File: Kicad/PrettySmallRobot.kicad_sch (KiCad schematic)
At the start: 52 parts, among them J1 TYPE-C-31-M-12, J2 S2B-PH-K-S(LF)(SN), J3 S2B-PH-K-S(LF)(SN), J4 S2B-PH-K-S(LF)(SN), SW1 SW_Push, SW2 SW_Push, U1 DRV8837, U2 DRV8837, U3 MCP73831-2ACI_MC, U4 ESP32-S2

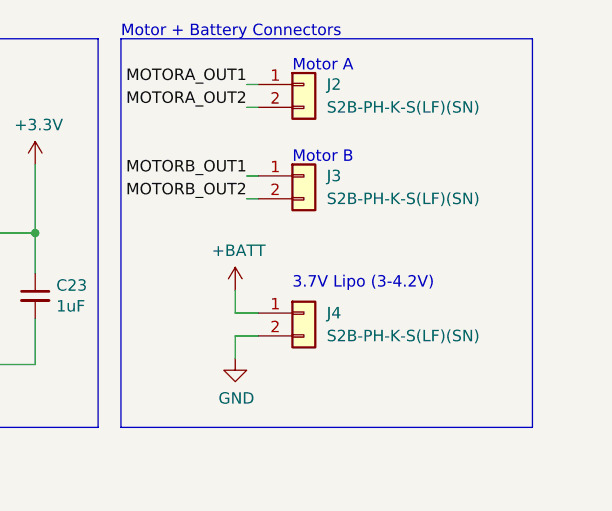
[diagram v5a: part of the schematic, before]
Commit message: replaced jst connectors with smd solder pads
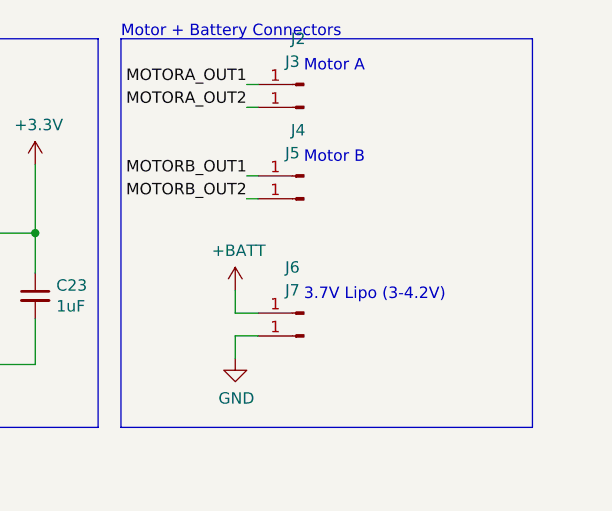
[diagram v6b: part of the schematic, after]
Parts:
- removed J2, J3, J4: S2B-PH-K-S(LF)(SN), Connector_JST:JST_PH_S2B-PH-K_1x02_P2.00mm_Horizontal, symbol Connector_Generic:Conn_01x02
- added J2, J3, J4, J5, J6, J7: (no value), Connector_Wire:SolderWirePad_1x01_SMD_1x2mm, symbol Connector:Conn_01x01_Male
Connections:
- net +BATT: now also J6.1 (Pin_1)
- net GND: now also J7.1 (Pin_1)
- net MOTORA_OUT1: now also J2.1 (Pin_1)
- net MOTORA_OUT2: now also J3.1 (Pin_1)
- net MOTORB_OUT1: now also J4.1 (Pin_1)
- net MOTORB_OUT2: now also J5.1 (Pin_1)
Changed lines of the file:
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@@
     (effects (font (size 1.27 1.27)) (justify left bottom))
   )
-  (text "Motor A" (at 254 20.32 0)
+  (text "Motor A" (at 255.27 20.32 0)
     (effects (font (size 1.27 1.27)) (justify left bottom))
   )
@@
     (effects (font (size 1.27 1.27)) (justify left bottom))
   )
-  (text "Motor B" (at 254 30.48 0)
+  (text "Motor B" (at 255.27 30.48 0)
     (effects (font (size 1.27 1.27)) (justify left bottom))
   )
-  (text "3.7V Lipo (3-4.2V)" (at 254 44.45 0)
+  (text "3.7V Lipo (3-4.2V)" (at 255.27 45.72 0)
     (effects (font (size 1.27 1.27)) (justify left bottom))
   )
@@
   (label "VDD3P3" (at 44.45 179.07 270)
     (effects (font (size 1.27 1.27)) (justify right bottom))
+  )
+  (symbol (lib_id "Connector:Conn_01x01_Male") (at 255.27 49.53 180) (unit 1)
+    (in_bom yes) (on_board yes)
+    (property "Reference" "J7" (id 0) (at 254 44.45 0))
+    (property "Value" "" (id 1) (at 257.81 49.53 0))
+    (property "Footprint" "Connector_Wire:SolderWirePad_1x01_SMD_1x2mm" (id 2) (at 255.27 49.53 0)
+      (effects (font (size 1.27 1.27)) hide)
+    )
+    (property "Datasheet" "~" (id 3) (at 255.27 49.53 0)
+      (effects (font (size 1.27 1.27)) hide)
+    )
+    (pin "1")
   )
   (symbol (lib_id "power:GND") (at 207.01 52.705 0) (unit 1)
@@
     (pin "1")
     (pin "2")
+  )
+  (symbol (lib_id "Connector:Conn_01x01_Male") (at 255.27 46.99 180) (unit 1)
+    (in_bom yes) (on_board yes)
+    (property "Reference" "J6" (id 0) (at 254 41.91 0))
+    (property "Value" "" (id 1) (at 259.08 46.99 0))
+    (property "Footprint" "Connector_Wire:SolderWirePad_1x01_SMD_1x2mm" (id 2) (at 255.27 46.99 0)
+      (effects (font (size 1.27 1.27)) hide)
+    )
+    (property "Datasheet" "~" (id 3) (at 255.27 46.99 0)
+      (effects (font (size 1.27 1.27)) hide)
+    )
+    (pin "1")
   )
   (symbol (lib_id "power:GND") (at 119.38 127 90) (unit 1)
@@
     (pin "2")
   )
-  (symbol (lib_id "Connector_Generic:Conn_01x02") (at 255.27 21.59 0) (unit 1)
-    (in_bom yes) (on_board yes) (fields_autoplaced)
-    (property "Reference" "J2" (id 0) (at 257.81 21.5899 0)
-      (effects (font (size 1.27 1.27)) (justify left))
-    )
-    (property "Value" "S2B-PH-K-S(LF)(SN)" (id 1) (at 257.81 24.1299 0)
-      (effects (font (size 1.27 1.27)) (justify left))
-    )
-    (property "Footprint" "Connector_JST:JST_PH_S2B-PH-K_1x02_P2.00mm_Horizontal" (id 2) (at 255.27 21.59 0)
-      (effects (font (size 1.27 1.27)) hide)
-    )
-    (property "Datasheet" "~" (id 3) (at 255.27 21.59 0)
-      (effects (font (size 1.27 1.27)) hide)
-    )
-    (property "LCSC" "C173752" (id 4) (at 255.27 21.59 0)
-      (effects (font (size 1.27 1.27)) hide)
-    )
-    (pin "1")
-    (pin "2")
-  )
   (symbol (lib_id "power:+3.3V") (at 54.61 176.53 0) (unit 1)
     (in_bom yes) (on_board yes)
@@
     (pin "2")
   )
-  (symbol (lib_id "Connector_Generic:Conn_01x02") (at 255.27 46.99 0) (unit 1)
-    (in_bom yes) (on_board yes) (fields_autoplaced)
-    (property "Reference" "J4" (id 0) (at 257.81 46.9899 0)
-      (effects (font (size 1.27 1.27)) (justify left))
-    )
-    (property "Value" "S2B-PH-K-S(LF)(SN)" (id 1) (at 257.81 49.5299 0)
-      (effects (font (size 1.27 1.27)) (justify left))
-    )
-    (property "Footprint" "Connector_JST:JST_PH_S2B-PH-K_1x02_P2.00mm_Horizontal" (id 2) (at 255.27 46.99 0)
-      (effects (font (size 1.27 1.27)) hide)
-    )
-    (property "Datasheet" "~" (id 3) (at 255.27 46.99 0)
-      (effects (font (size 1.27 1.27)) hide)
-    )
-    (property "LCSC" "C173752" (id 4) (at 255.27 46.99 0)
-      (effects (font (size 1.27 1.27)) hide)
-    )
-    (pin "1")
-    (pin "2")
+  (symbol (lib_id "Connector:Conn_01x01_Male") (at 255.27 24.13 180) (unit 1)
+    (in_bom yes) (on_board yes)
+    (property "Reference" "J3" (id 0) (at 254 19.05 0))
+    (property "Value" "" (id 1) (at 260.35 24.13 0))
+    (property "Footprint" "Connector_Wire:SolderWirePad_1x01_SMD_1x2mm" (id 2) (at 255.27 24.13 0)
+      (effects (font (size 1.27 1.27)) hide)
+    )
+    (property "Datasheet" "~" (id 3) (at 255.27 24.13 0)
+      (effects (font (size 1.27 1.27)) hide)
+    )
+    (pin "1")
   )
   (symbol (lib_id "power:+3.3V") (at 67.31 176.53 0) (unit 1)
@@
     )
     (property "Datasheet" "" (id 3) (at 86.36 46.99 0)
+      (effects (font (size 1.27 1.27)) hide)
+    )
+    (pin "1")
+  )
+  (symbol (lib_id "Connector:Conn_01x01_Male") (at 255.27 21.59 180) (unit 1)
+    (in_bom yes) (on_board yes)
+    (property "Reference" "J2" (id 0) (at 254.635 16.51 0))
+    (property "Value" "" (id 1) (at 260.35 21.59 0))
+    (property "Footprint" "Connector_Wire:SolderWirePad_1x01_SMD_1x2mm" (id 2) (at 255.27 21.59 0)
+      (effects (font (size 1.27 1.27)) hide)
+    )
+    (property "Datasheet" "~" (id 3) (at 255.27 21.59 0)
       (effects (font (size 1.27 1.27)) hide)
     )
@@
     (pin "9")
   )
-  (symbol (lib_id "Connector_Generic:Conn_01x02") (at 255.27 31.75 0) (unit 1)
-    (in_bom yes) (on_board yes) (fields_autoplaced)
-    (property "Reference" "J3" (id 0) (at 257.81 31.7499 0)
-      (effects (font (size 1.27 1.27)) (justify left))
-    )
-    (property "Value" "S2B-PH-K-S(LF)(SN)" (id 1) (at 257.81 34.2899 0)
-      (effects (font (size 1.27 1.27)) (justify left))
-    )
-    (property "Footprint" "Connector_JST:JST_PH_S2B-PH-K_1x02_P2.00mm_Horizontal" (id 2) (at 255.27 31.75 0)
-      (effects (font (size 1.27 1.27)) hide)
-    )
-    (property "Datasheet" "~" (id 3) (at 255.27 31.75 0)
-      (effects (font (size 1.27 1.27)) hide)
-    )
-    (property "LCSC" "C173752" (id 4) (at 255.27 31.75 0)
-      (effects (font (size 1.27 1.27)) hide)
-    )
-    (pin "1")
-    (pin "2")
-  )
   (symbol (lib_id "power:+3.3V") (at 208.28 148.59 0) (unit 1)
     (in_bom yes) (on_board yes)
@@
     (pin "2")
   )
+  (symbol (lib_id "Connector:Conn_01x01_Male") (at 255.27 34.29 180) (unit 1)
+    (in_bom yes) (on_board yes)
+    (property "Reference" "J5" (id 0) (at 254 29.21 0))
+    (property "Value" "" (id 1) (at 260.35 34.29 0))
+    (property "Footprint" "Connector_Wire:SolderWirePad_1x01_SMD_1x2mm" (id 2) (at 255.27 34.29 0)
+      (effects (font (size 1.27 1.27)) hide)
+    )
+    (property "Datasheet" "~" (id 3) (at 255.27 34.29 0)
+      (effects (font (size 1.27 1.27)) hide)
+    )
+    (pin "1")
+  )
   (symbol (lib_id "Device:C_Small") (at 78.74 180.34 0) (unit 1)
     (in_bom yes) (on_board yes)
@@
     (pin "1")
     (pin "2")
+  )
+  (symbol (lib_id "Connector:Conn_01x01_Male") (at 255.27 31.75 180) (unit 1)
+    (in_bom yes) (on_board yes)
+    (property "Reference" "J4" (id 0) (at 254.635 26.67 0))
+    (property "Value" "" (id 1) (at 260.35 31.75 0))
+    (property "Footprint" "Connector_Wire:SolderWirePad_1x01_SMD_1x2mm" (id 2) (at 255.27 31.75 0)
+      (effects (font (size 1.27 1.27)) hide)
+    )
+    (property "Datasheet" "~" (id 3) (at 255.27 31.75 0)
+      (effects (font (size 1.27 1.27)) hide)
+    )
+    (pin "1")
   )
   (symbol (lib_id "Connector:TestPoint") (at 219.71 38.1 0) (unit 1)
@@
       (reference "J1") (unit 1) (value "TYPE-C-31-M-12") (footprint "kicad_footprints:HRO_TYPE-C-31-M-12")
     )
-    (path "/3df40196-e4fa-42be-bb30-c5850f257a4a"
-      (reference "J2") (unit 1) (value "S2B-PH-K-S(LF)(SN)") (footprint "Connector_JST:JST_PH_S2B-PH-K_1x02_P2.00mm_Horizontal")
-    )
-    (path "/8c3a71db-8570-4a26-8abb-7b253c8386f5"
-      (reference "J3") (unit 1) (value "S2B-PH-K-S(LF)(SN)") (footprint "Connector_JST:JST_PH_S2B-PH-K_1x02_P2.00mm_Horizontal")
-    )
-    (path "/6502a99f-049b-4441-92af-fda3c2641b16"
-      (reference "J4") (unit 1) (value "S2B-PH-K-S(LF)(SN)") (footprint "Connector_JST:JST_PH_S2B-PH-K_1x02_P2.00mm_Horizontal")
+    (path "/7a0e3aeb-7d38-4968-abed-3c937ea7d594"
+      (reference "J2") (unit 1) (value "MOTORA_1") (footprint "Connector_Wire:SolderWirePad_1x01_SMD_1x2mm")
+    )
+    (path "/66094016-cb8b-4def-bb4e-08ce9dbd32a0"
+      (reference "J3") (unit 1) (value "MOTORA_2") (footprint "Connector_Wire:SolderWirePad_1x01_SMD_1x2mm")
+    )
+    (path "/c4045a03-fc7b-44a0-8023-e7f7c172c253"
+      (reference "J4") (unit 1) (value "MOTORB_1") (footprint "Connector_Wire:SolderWirePad_1x01_SMD_1x2mm")
+    )
+    (path "/a6744a83-e2fe-461f-99f7-2067ecacb1f9"
+      (reference "J5") (unit 1) (value "MOTORB_2") (footprint "Connector_Wire:SolderWirePad_1x01_SMD_1x2mm")
+    )
+    (path "/25861b43-2ae6-4545-970c-1cadff460964"
+      (reference "J6") (unit 1) (value "BATT+") (footprint "Connector_Wire:SolderWirePad_1x01_SMD_1x2mm")
+    )
+    (path "/029525a0-8a41-486f-a02b-f13993394b49"
+      (reference "J7") (unit 1) (value "GND") (footprint "Connector_Wire:SolderWirePad_1x01_SMD_1x2mm")
     )
     (path "/705dc02d-e1e2-48cd-b58e-8d1e3dfceb42"

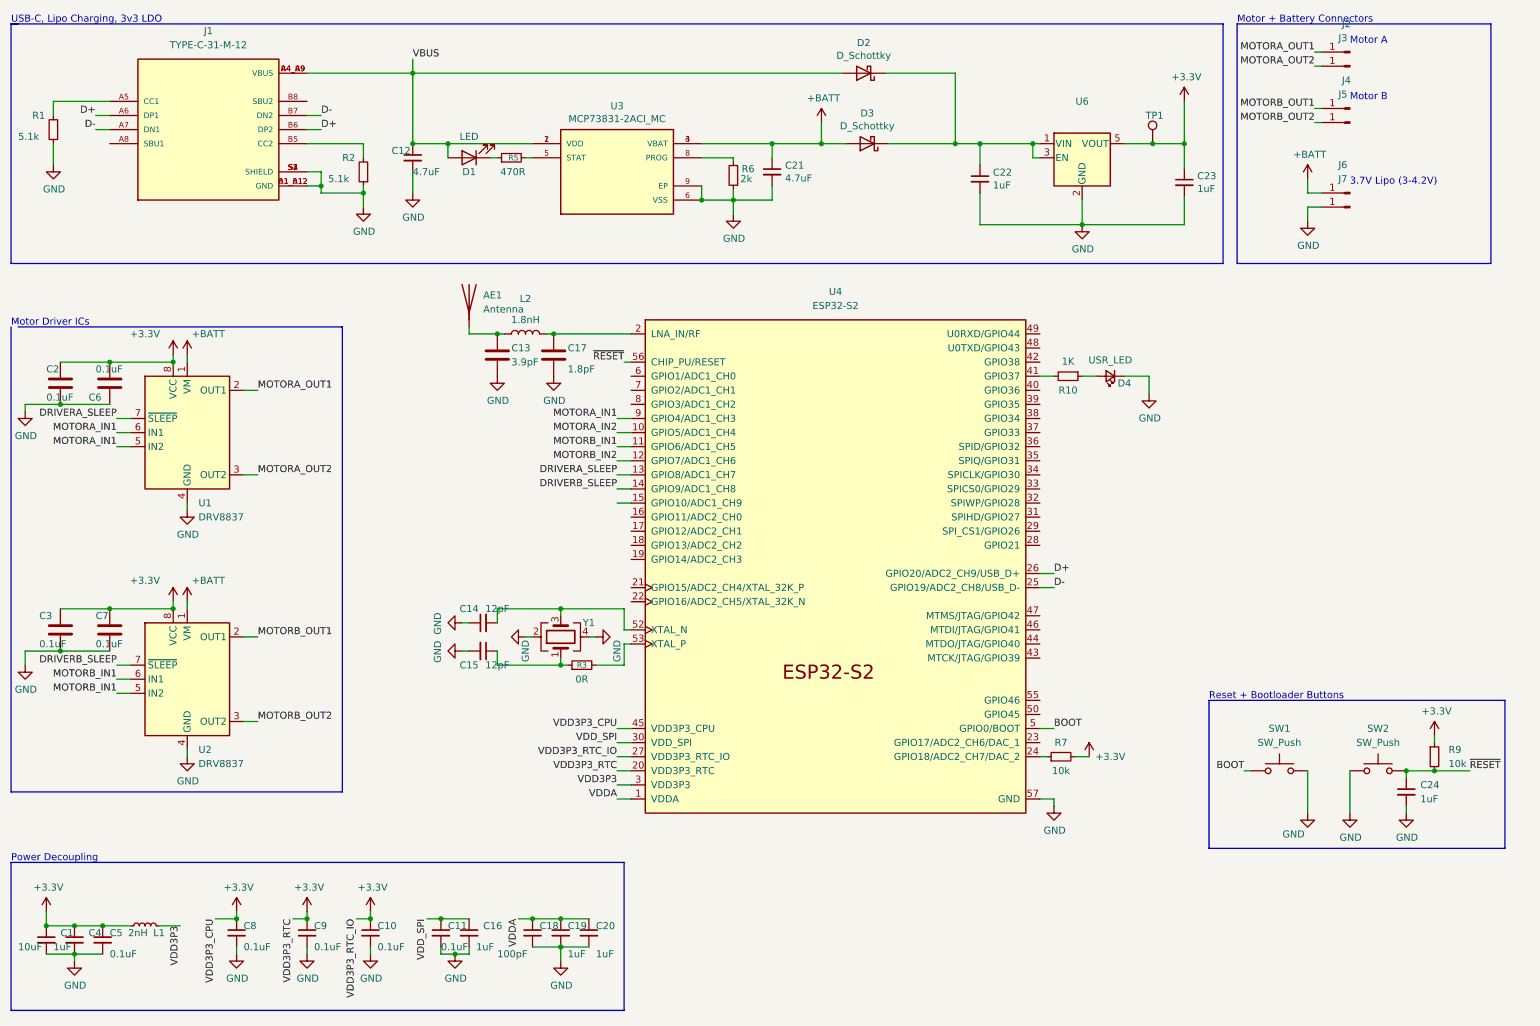
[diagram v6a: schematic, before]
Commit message: routed motor driver sigs
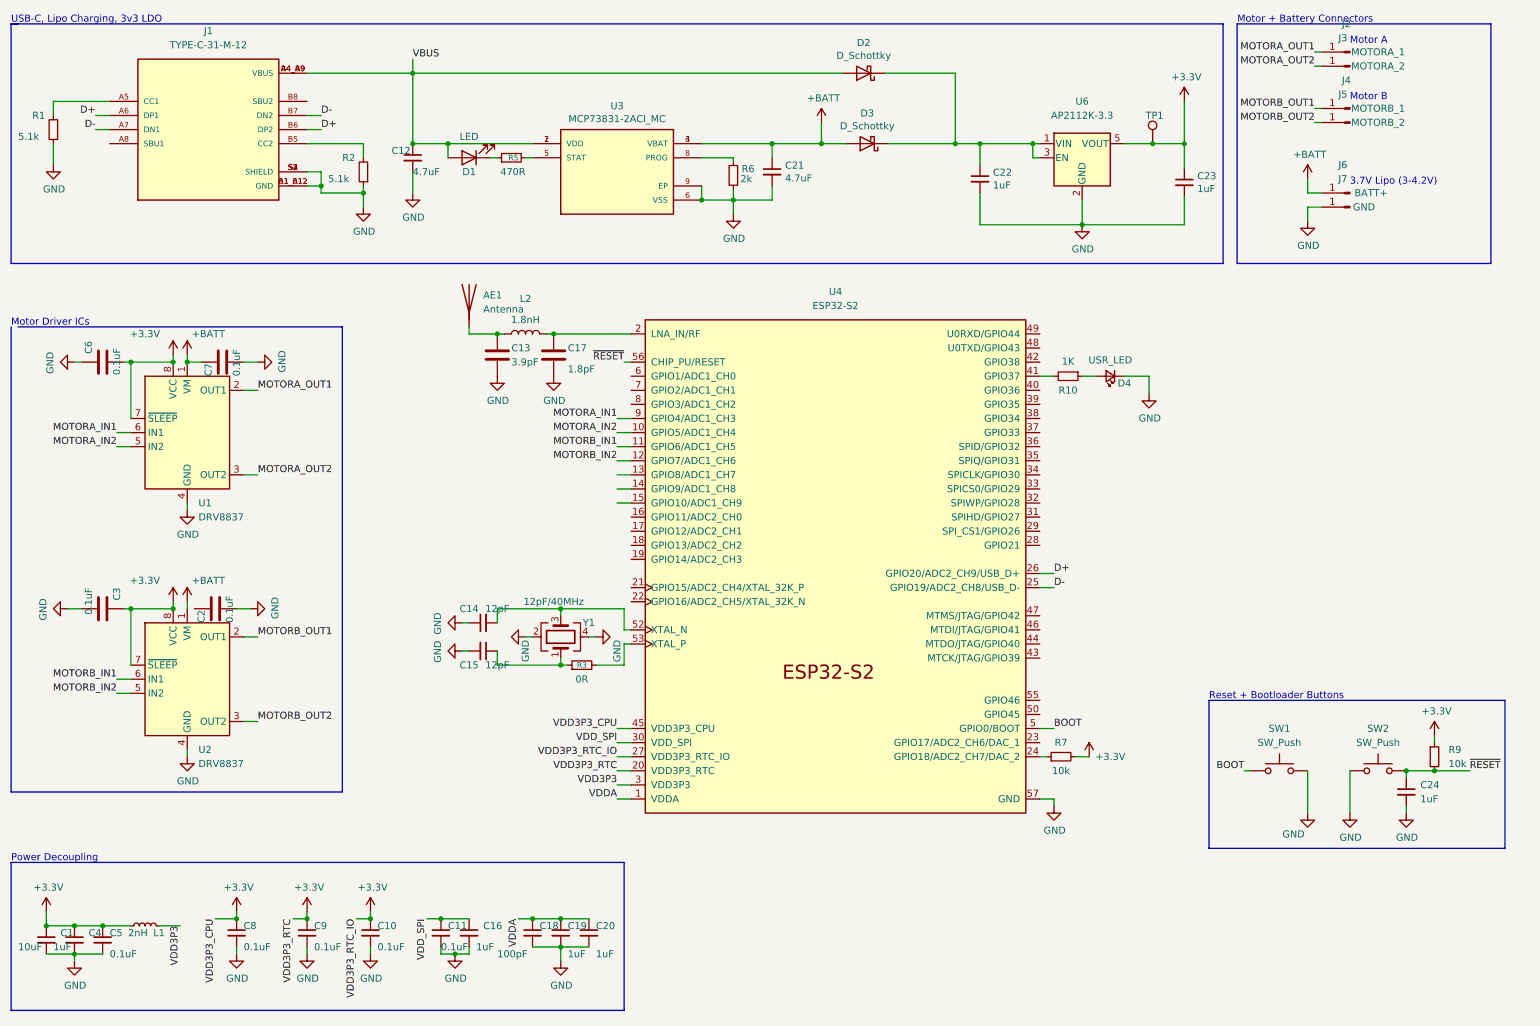
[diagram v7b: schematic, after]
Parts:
- J2: value (none) -> MOTORA_1
- J3: value (none) -> MOTORA_2
- J4: value (none) -> MOTORB_1
- J5: value (none) -> MOTORB_2
- J6: value (none) -> BATT+
- J7: value (none) -> GND
- U6: value (none) -> AP2112K-3.3; footprint (none) -> Package_TO_SOT_SMD:SOT-23-5
- Y1: value (none) -> 12pF/40MHz; footprint (none) -> Crystal:Crystal_SMD_3225-4Pin_3.2x2.5mm
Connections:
- net +3V3: now also U1.7 (~{SLEEP}), U2.7 (~{SLEEP}); no longer C2.1, C7.1
- net +BATT: now also C7.1
- net MOTORA_IN1: no longer U1.5 (IN2)
- net MOTORA_IN2: now also U1.5 (IN2)
- net MOTORB_IN1: no longer U2.5 (IN2)
- net MOTORB_IN2: now also U2.5 (IN2)
- net DRIVERA_SLEEP: no longer names the net of U4.13 (GPIO8/ADC1_CH7)
- net DRIVERA_SLEEP: no longer U1.7 (~{SLEEP})
- net DRIVERB_SLEEP: no longer names the net of U4.14 (GPIO9/ADC1_CH8)
- net DRIVERB_SLEEP: no longer U2.7 (~{SLEEP})
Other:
- moved on the sheet: C3, C6
